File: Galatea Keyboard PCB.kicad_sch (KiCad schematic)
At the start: 0 parts

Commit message: Updated the net labels for 3v3 and sys rail
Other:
- sheet MCU SECTION ports: added VADC, usb_vbus_det; removed none
- sheet POWER SECTION ports: added I2C0_SCL, I2C0_SDA, VADC, usb_vbus_det; removed none
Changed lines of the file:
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@@
+	)
+	(junction
+		(at 121.92 78.74)
+		(diameter 0)
+		(color 0 0 0 0)
 	)
 	(junction
@@
 		(color 0 0 0 0)
 	)
+	(junction
+		(at 114.3 74.93)
+		(diameter 0)
+		(color 0 0 0 0)
+	)
 	(wire
 		(pts
@@
 	(wire
 		(pts
+			(xy 69.85 78.74) (xy 121.92 78.74)
+		)
+		(stroke
+			(width 0)
+			(type default)
+		)
+	)
+	(wire
+		(pts
 			(xy 210.82 135.89) (xy 210.82 145.796)
 		)
@@
 	(wire
 		(pts
+			(xy 62.23 74.93) (xy 114.3 74.93)
+		)
+		(stroke
+			(width 0)
+			(type default)
+		)
+	)
+	(wire
+		(pts
 			(xy 207.01 84.836) (xy 207.01 74.676)
 		)
@@
 	(wire
 		(pts
+			(xy 62.23 85.09) (xy 62.23 74.93)
+		)
+		(stroke
+			(width 0)
+			(type default)
+		)
+	)
+	(wire
+		(pts
 			(xy 154.94 135.89) (xy 154.94 145.796)
 		)
@@
 	(wire
 		(pts
+			(xy 114.3 74.93) (xy 114.3 84.328)
+		)
+		(stroke
+			(width 0)
+			(type default)
+		)
+	)
+	(wire
+		(pts
 			(xy 162.56 140.716) (xy 203.2 140.716)
 		)
@@
 	(wire
 		(pts
-			(xy 114.3 64.77) (xy 114.3 84.328)
+			(xy 114.3 64.77) (xy 114.3 74.93)
 		)
 		(stroke
@@
 	(wire
 		(pts
+			(xy 77.47 124.46) (xy 85.344 124.46)
+		)
+		(stroke
+			(width 0)
+			(type default)
+		)
+	)
+	(wire
+		(pts
 			(xy 175.006 122.936) (xy 188.214 122.936)
 		)
@@
 	(wire
 		(pts
+			(xy 69.85 85.09) (xy 69.85 78.74)
+		)
+		(stroke
+			(width 0)
+			(type default)
+		)
+	)
+	(wire
+		(pts
 			(xy 148.59 64.77) (xy 148.59 74.676)
 		)
@@
 		(pts
 			(xy 125.73 135.89) (xy 125.73 155.956)
+		)
+		(stroke
+			(width 0)
+			(type default)
+		)
+	)
+	(wire
+		(pts
+			(xy 77.47 118.11) (xy 85.344 118.11)
 		)
 		(stroke
@@
 			)
 		)
+		(pin "usb_vbus_det" input
+			(at 85.344 118.11 180)
+			(effects
+				(font
+					(size 1.27 1.27)
+				)
+				(justify left)
+			)
+		)
+		(pin "VADC" passive
+			(at 85.344 124.46 180)
+			(effects
+				(font
+					(size 1.27 1.27)
+				)
+				(justify left)
+			)
+		)
 		(instances
 			(project "Galatea Keyboard PCB"
@@
 			(effects
 				(font
+					(size 1.27 1.27)
+				)
+				(justify right)
+			)
+		)
+		(pin "I2C0_SCL" input
+			(at 62.23 85.09 90)
+			(effects
+				(font
+					(size 1.27 1.27)
+				)
+				(justify right)
+			)
+		)
+		(pin "I2C0_SDA" input
+			(at 69.85 85.09 90)
+			(effects
+				(font
+					(size 1.27 1.27)
+				)
+				(justify right)
+			)
+		)
+		(pin "usb_vbus_det" input
+			(at 77.47 118.11 0)
+			(effects
+				(font
+					(size 1.27 1.27)
+				)
+				(justify right)
+			)
+		)
+		(pin "VADC" passive
+			(at 77.47 124.46 0)
+			(effects
+				(font

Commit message: Progress on the PCB routing
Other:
- sheet MCU SECTION ports: added DSI_CLK_N, DSI_CLK_P, DSI_DATA0_N, DSI_DATA0_P, DSI_DATA1_N, DSI_DATA1_P; removed DSI_CLKN, DSI_CLKP, DSI_DATAN0, DSI_DATAN1, DSI_DATAP0, DSI_DATAP1
- sheet ROTARY, TACT SWITCH AND LCD ports: added DSI_CLK_N, DSI_CLK_P, DSI_DATA0_N, DSI_DATA0_P, DSI_DATA1_N, DSI_DATA1_P; removed DSI_CLKN, DSI_CLKP, DSI_DATAN0, DSI_DATAN1, DSI_DATAP0, DSI_DATAP1
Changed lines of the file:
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@@
+	(wire
+		(pts
+			(xy 175.006 130.81) (xy 188.214 130.81)
+		)
+		(stroke
+			(width 0)
+			(type default)
+		)
+	)
 	(wire
 		(pts
@@
 	(wire
 		(pts
-			(xy 175.006 126.746) (xy 188.214 126.746)
-		)
-		(stroke
-			(width 0)
-			(type default)
-		)
-	)
-	(wire
-		(pts
 			(xy 175.006 115.316) (xy 188.214 115.316)
 		)
@@
 	(wire
 		(pts
+			(xy 175.006 127) (xy 188.214 127)
+		)
+		(stroke
+			(width 0)
+			(type default)
+		)
+	)
+	(wire
+		(pts
 			(xy 162.56 135.89) (xy 162.56 140.716)
 		)
@@
 		(pts
 			(xy 133.35 135.89) (xy 133.35 155.956)
-		)
-		(stroke
-			(width 0)
-			(type default)
-		)
-	)
-	(wire
-		(pts
-			(xy 175.006 130.556) (xy 188.214 130.556)
 		)
 		(stroke
@@
 			)
 		)
-		(pin "DSI_CLKN" output
-			(at 175.006 130.556 0)
-			(effects
-				(font
-					(size 1.27 1.27)
-				)
-				(justify right)
-			)
-		)
-		(pin "DSI_CLKP" output
-			(at 175.006 126.746 0)
-			(effects
-				(font
-					(size 1.27 1.27)
-				)
-				(justify right)
-			)
-		)
-		(pin "DSI_DATAN0" output
-			(at 151.13 135.89 270)
-			(effects
-				(font
-					(size 1.27 1.27)
-				)
-				(justify left)
-			)
-		)
-		(pin "DSI_DATAN1" output
-			(at 154.94 135.89 270)
-			(effects
-				(font
-					(size 1.27 1.27)
-				)
-				(justify left)
-			)
-		)
-		(pin "DSI_DATAP0" output
-			(at 147.32 135.89 270)
-			(effects
-				(font
-					(size 1.27 1.27)
-				)
-				(justify left)
-			)
-		)
-		(pin "DSI_DATAP1" output
-			(at 158.75 135.89 270)
-			(effects
-				(font
-					(size 1.27 1.27)
-				)
-				(justify left)
-			)
-		)
 		(pin "LCD_BL_PWM" input
 			(at 162.56 135.89 270)
@@
 		(pin "VADC" passive
 			(at 85.344 124.46 180)
+			(effects
+				(font
+					(size 1.27 1.27)
+				)
+				(justify left)
+			)
+		)
+		(pin "DSI_DATA0_N" output
+			(at 151.13 135.89 270)
+			(effects
+				(font
+					(size 1.27 1.27)
+				)
+				(justify left)
+			)
+		)
+		(pin "DSI_DATA0_P" output
+			(at 147.32 135.89 270)
+			(effects
+				(font
+					(size 1.27 1.27)
+				)
+				(justify left)
+			)
+		)
+		(pin "DSI_CLK_N" output
+			(at 175.006 127 0)
+			(effects
+				(font
+					(size 1.27 1.27)
+				)
+				(justify right)
+			)
+		)
+		(pin "DSI_CLK_P" output
+			(at 175.006 130.81 0)
+			(effects
+				(font
+					(size 1.27 1.27)
+				)
+				(justify right)
+			)
+		)
+		(pin "DSI_DATA1_N" output
+			(at 154.94 135.89 270)
+			(effects
+				(font
+					(size 1.27 1.27)
+				)
+				(justify left)
+			)
+		)
+		(pin "DSI_DATA1_P" output
+			(at 158.75 135.89 270)
 			(effects
 				(font
@@
 			)
 		)
-		(pin "DSI_CLKN" input
-			(at 188.214 126.746 180)
-			(effects
-				(font
-					(size 1.27 1.27)
-				)
-				(justify left)
-			)
-		)
-		(pin "DSI_CLKP" input
-			(at 188.214 130.556 180)
-			(effects
-				(font
-					(size 1.27 1.27)
-				)
-				(justify left)
-			)
-		)
-		(pin "DSI_DATAN0" input
-			(at 214.63 135.89 270)
-			(effects
-				(font
-					(size 1.27 1.27)
-				)
-				(justify left)
-			)
-		)
-		(pin "DSI_DATAN1" input
-			(at 210.82 135.89 270)
-			(effects
-				(font
-					(size 1.27 1.27)
-				)
-				(justify left)
-			)
-		)
-		(pin "DSI_DATAP0" input
-			(at 218.44 135.89 270)
-			(effects
-				(font
-					(size 1.27 1.27)
-				)
-				(justify left)
-			)
-		)
-		(pin "DSI_DATAP1" input
-			(at 207.01 135.89 270)
-			(effects
-				(font
-					(size 1.27 1.27)
-				)
-				(justify left)
-			)
-		)
 		(pin "LCD_BL_PWM" input
 			(at 203.2 135.89 270)
 			(effects
 				(font
+					(size 1.27 1.27)
+				)
+				(justify left)
+			)
+		)
+		(pin "DSI_DATA0_N" input
+			(at 214.63 135.89 270)
+			(effects
+				(font
+					(size 1.27 1.27)
+				)
+				(justify left)
+			)
+		)
+		(pin "DSI_DATA0_P" input
+			(at 218.44 135.89 270)
+			(effects
+				(font
+					(size 1.27 1.27)
+				)
+				(justify left)
+			)
+		)
+		(pin "DSI_CLK_N" input
+			(at 188.214 127 180)
+			(effects
+				(font
+					(size 1.27 1.27)
+				)
+				(justify left)
+			)
+		)
+		(pin "DSI_CLK_P" input
+			(at 188.214 130.81 180)
+			(effects
+				(font
+					(size 1.27 1.27)
+				)
+				(justify left)
+			)
+		)
+		(pin "DSI_DATA1_N" input
+			(at 210.82 135.89 270)
+			(effects
+				(font
+					(size 1.27 1.27)
+				)
+				(justify left)
+			)
+		)
+		(pin "DSI_DATA1_P" input
+			(at 207.01 135.89 270)
+			(effects
+				(font

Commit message: Done with the correction, PCB is complete
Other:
- sheet MCU SECTION ports: added ALERT; removed none
- sheet POWER SECTION ports: added ALERT; removed none
- sheet ROTARY, TACT SWITCH AND LCD ports: added I2C0_SCL, I2C0_SDA; removed I2C1_SCL, I2C1_SDA

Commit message: Corrected the issues raised
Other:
- sheet MCU SECTION ports: added LCD_RESET; removed none
- sheet ROTARY, TACT SWITCH AND LCD ports: added LCD_RESET; removed none
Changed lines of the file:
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@@
+	(wire
+		(pts
+			(xy 175.006 101.6) (xy 188.214 101.6)
+		)
+		(stroke
+			(width 0)
+			(type default)
+		)
+	)
 	(wire
 		(pts
@@
 			)
 		)
+		(pin "LCD_RESET" input
+			(at 175.006 101.6 0)
+			(effects
+				(font
+					(size 1.27 1.27)
+				)
+				(justify right)
+			)
+		)
 		(instances
 			(project "Galatea Keyboard PCB"
@@
 			)
 		)
+		(pin "LCD_RESET" input
+			(at 188.214 101.6 180)
+			(effects
+				(font
+					(size 1.27 1.27)
+				)
+				(justify left)
+			)
+		)

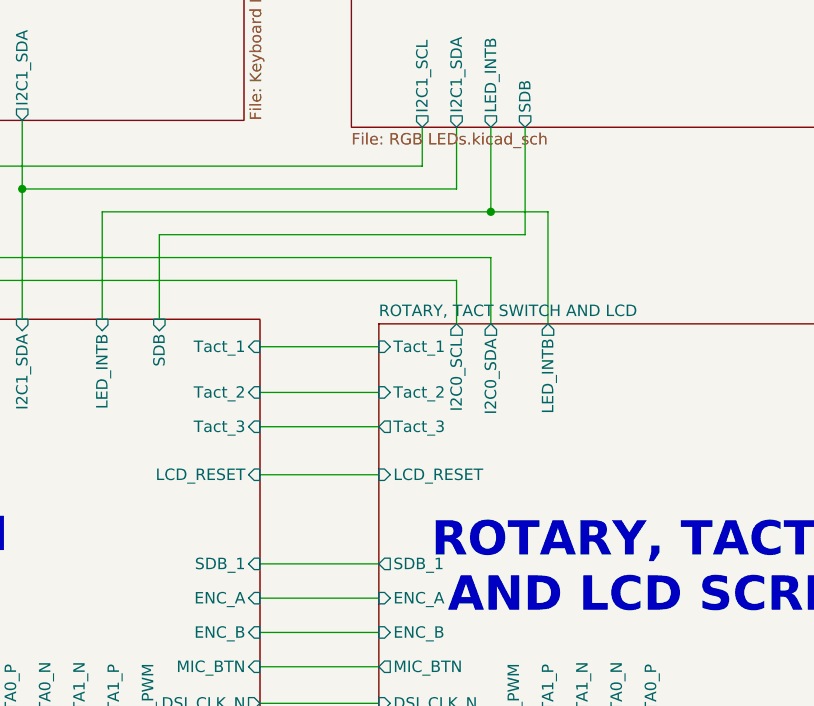
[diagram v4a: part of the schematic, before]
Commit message: Added GT911 connector and fix the USB_C issue
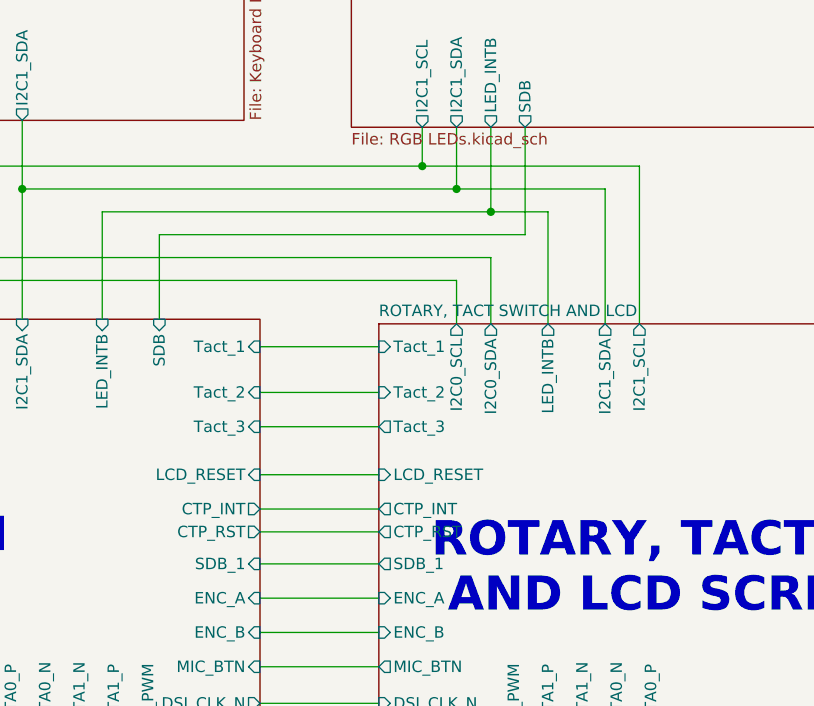
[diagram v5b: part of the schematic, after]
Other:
- sheet MCU SECTION ports: added CTP_INT, CTP_RST; removed none
- sheet ROTARY, TACT SWITCH AND LCD ports: added CTP_INT, CTP_RST, I2C1_SCL, I2C1_SDA; removed none
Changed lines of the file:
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@@
+	)
+	(junction
+		(at 193.04 67.31)
+		(diameter 0)
+		(color 0 0 0 0)
 	)
 	(junction
@@
 		(color 0 0 0 0)
 	)
+	(junction
+		(at 196.85 69.85)
+		(diameter 0)
+		(color 0 0 0 0)
+	)
 	(wire
 		(pts
@@
 	(wire
 		(pts
+			(xy 213.36 69.85) (xy 196.85 69.85)
+		)
+		(stroke
+			(width 0)
+			(type default)
+		)
+	)
+	(wire
+		(pts
 			(xy 175.006 119.126) (xy 188.214 119.126)
 		)
@@
 	(wire
 		(pts
+			(xy 217.17 67.31) (xy 193.04 67.31)
+		)
+		(stroke
+			(width 0)
+			(type default)
+		)
+	)
+	(wire
+		(pts
 			(xy 200.66 62.992) (xy 200.66 72.39)
 		)
@@
 	(wire
 		(pts
+			(xy 175.006 105.41) (xy 188.214 105.41)
+		)
+		(stroke
+			(width 0)
+			(type default)
+		)
+	)
+	(wire
+		(pts
 			(xy 157.48 72.39) (xy 200.66 72.39)
 		)
@@
 	(wire
 		(pts
+			(xy 213.36 84.836) (xy 213.36 69.85)
+		)
+		(stroke
+			(width 0)
+			(type default)
+		)
+	)
+	(wire
+		(pts
 			(xy 175.006 115.316) (xy 188.214 115.316)
 		)
@@
 	(wire
 		(pts
+			(xy 175.006 107.95) (xy 188.214 107.95)
+		)
+		(stroke
+			(width 0)
+			(type default)
+		)
+	)
+	(wire
+		(pts
 			(xy 114.3 74.93) (xy 114.3 84.328)
 		)
@@
 		(pts
 			(xy 133.35 135.89) (xy 133.35 155.956)
+		)
+		(stroke
+			(width 0)
+			(type default)
+		)
+	)
+	(wire
+		(pts
+			(xy 217.17 84.836) (xy 217.17 67.31)
 		)
 		(stroke
@@
 			)
 		)
+		(pin "CTP_INT" output
+			(at 175.006 105.41 0)
+			(effects
+				(font
+					(size 1.27 1.27)
+				)
+				(justify right)
+			)
+		)
+		(pin "CTP_RST" output
+			(at 175.006 107.95 0)
+			(effects
+				(font
+					(size 1.27 1.27)
+				)
+				(justify right)
+			)
+		)
 		(instances
 			(project "Galatea Keyboard PCB"
@@
 			)
 		)
+		(pin "CTP_INT" output
+			(at 188.214 105.41 180)
+			(effects
+				(font
+					(size 1.27 1.27)
+				)
+				(justify left)
+			)
+		)
+		(pin "CTP_RST" output
+			(at 188.214 107.95 180)
+			(effects
+				(font
+					(size 1.27 1.27)
+				)
+				(justify left)
+			)
+		)
+		(pin "I2C1_SCL" output
+			(at 217.17 84.836 90)
+			(effects
+				(font
+					(size 1.27 1.27)
+				)
+				(justify right)
+			)
+		)
+		(pin "I2C1_SDA" output
+			(at 213.36 84.836 90)
+			(effects
+				(font
+					(size 1.27 1.27)
+				)
+				(justify right)
+			)
+		)
